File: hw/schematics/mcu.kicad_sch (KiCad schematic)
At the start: 10 parts, among them J3 TC2050-IDC, U1 ISP2454-LP-JT

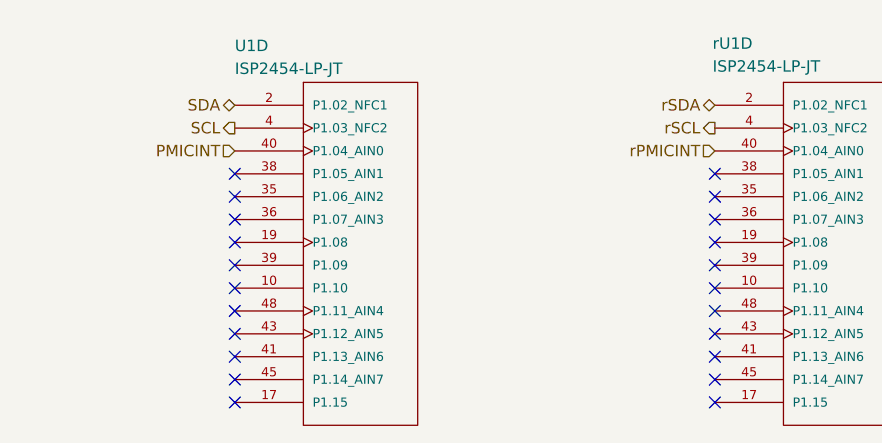
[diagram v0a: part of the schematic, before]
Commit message: Hook up matrix
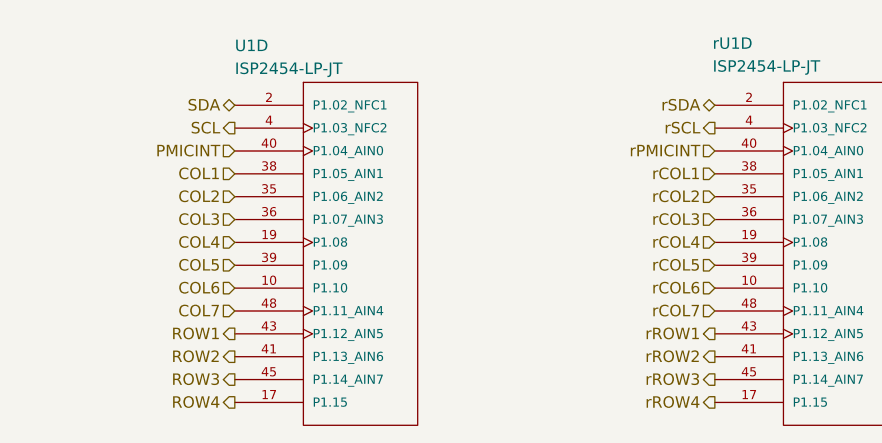
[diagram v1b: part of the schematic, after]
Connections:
- net COL6: now reaches U1.10 (P1.10)
- net ROW4: now reaches U1.17 (P1.15)
- net COL4: now reaches U1.19 (P1.08)
- net COL2: now reaches U1.35 (P1.06_AIN2)
- net COL3: now reaches U1.36 (P1.07_AIN3)
- net COL1: now reaches U1.38 (P1.05_AIN1)
- net COL5: now reaches U1.39 (P1.09)
- net ROW2: now reaches U1.41 (P1.13_AIN6)
- net ROW1: now reaches U1.43 (P1.12_AIN5)
- net ROW3: now reaches U1.45 (P1.14_AIN7)
- net COL7: now reaches U1.48 (P1.11_AIN4)
- net rCOL6: now reaches rU1.10 (P1.10)
- net rROW4: now reaches rU1.17 (P1.15)
- net rCOL4: now reaches rU1.19 (P1.08)
- net rCOL2: now reaches rU1.35 (P1.06_AIN2)
- net rCOL3: now reaches rU1.36 (P1.07_AIN3)
- net rCOL1: now reaches rU1.38 (P1.05_AIN1)
- net rCOL5: now reaches rU1.39 (P1.09)
- net rROW2: now reaches rU1.41 (P1.13_AIN6)
- net rROW1: now reaches rU1.43 (P1.12_AIN5)
- net rROW3: now reaches rU1.45 (P1.14_AIN7)
- net rCOL7: now reaches rU1.48 (P1.11_AIN4)
- no-connect marks 68 -> 46

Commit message: Annotate; Remove unused LDO/LS; Add RGB LED to PMIC
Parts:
- renumbered R15 to R12, R16 to R13, R17 to R14, rR15 to rR12, rR16 to rR13, rR17 to rR14
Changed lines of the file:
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@@
 		(on_board yes)
 		(dnp no)
-		(property "Reference" "rR15"
+		(property "Reference" "rR12"
 			(at 135.382 153.416 0)
 			(effects
@@
 			(project "alidade"
 				(path "/4cc5d416-57f5-4147-8183-e03ae6b1198a/43e81299-cad2-4202-975b-6352d1fdfcdc"
-					(reference "rR15")
+					(reference "rR12")
 					(unit 1)
 				)
@@
 		(on_board yes)
 		(dnp no)
-		(property "Reference" "rR17"
+		(property "Reference" "rR14"
 			(at 148.082 153.416 0)
 			(effects
@@
 			(project "alidade"
 				(path "/4cc5d416-57f5-4147-8183-e03ae6b1198a/43e81299-cad2-4202-975b-6352d1fdfcdc"
-					(reference "rR17")
+					(reference "rR14")
 					(unit 1)
 				)
@@
 		(on_board yes)
 		(dnp no)
-		(property "Reference" "rR16"
+		(property "Reference" "rR13"
 			(at 141.732 153.416 0)
 			(effects
@@
 			(project "alidade"
 				(path "/4cc5d416-57f5-4147-8183-e03ae6b1198a/43e81299-cad2-4202-975b-6352d1fdfcdc"
-					(reference "rR16")
+					(reference "rR13")
 					(unit 1)
 				)
@@
 		(on_board yes)
 		(dnp no)
-		(property "Reference" "R16"
+		(property "Reference" "R13"
 			(at 62.992 154.686 0)
 			(effects
@@
 			(project "alidade"
 				(path "/4cc5d416-57f5-4147-8183-e03ae6b1198a/43e81299-cad2-4202-975b-6352d1fdfcdc"
-					(reference "R16")
+					(reference "R13")
 					(unit 1)
 				)
@@
 		(on_board yes)
 		(dnp no)
-		(property "Reference" "R17"
+		(property "Reference" "R14"
 			(at 69.342 154.686 0)
 			(effects
@@
 			(project "alidade"
 				(path "/4cc5d416-57f5-4147-8183-e03ae6b1198a/43e81299-cad2-4202-975b-6352d1fdfcdc"
-					(reference "R17")
+					(reference "R14")
 					(unit 1)
 				)
@@
 		(on_board yes)
 		(dnp no)
-		(property "Reference" "R15"
+		(property "Reference" "R12"
 			(at 56.642 154.686 0)
 			(effects
@@
 			(project "alidade"
 				(path "/4cc5d416-57f5-4147-8183-e03ae6b1198a/43e81299-cad2-4202-975b-6352d1fdfcdc"
-					(reference "R15")
+					(reference "R12")
 					(unit 1)
 				)

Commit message: Rename power rails
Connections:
- net 1V8 renamed DVDD
- net r1V8 renamed rDVDD
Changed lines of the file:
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@@
 	)
 	(symbol
-		(lib_id "Alidade:r1V8")
+		(lib_id "Alidade:rDVDD")
 		(at 167.64 142.24 0)
 		(unit 1)
@@
 		(dnp no)
 		(fields_autoplaced yes)
-		(property "Reference" "#r1V8_08"
+		(property "Reference" "#rDVDD0110"
 			(at 167.64 146.05 0)
 			(effects
@@
 			)
 		)
-		(property "Value" "r1V8"
+		(property "Value" "rDVDD"
 			(at 167.64 137.16 0)
 			(effects
@@
 			(project "alidade"
 				(path "/4cc5d416-57f5-4147-8183-e03ae6b1198a/43e81299-cad2-4202-975b-6352d1fdfcdc"
-					(reference "#r1V8_08")
+					(reference "#rDVDD0110")
 					(unit 1)
 				)
@@
 	)
 	(symbol
-		(lib_id "Alidade:r1V8")
+		(lib_id "Alidade:rDVDD")
 		(at 80.01 44.45 0)
 		(unit 1)
@@
 		(dnp no)
 		(fields_autoplaced yes)
-		(property "Reference" "#r1V8_06"
+		(property "Reference" "#rDVDD0108"
 			(at 80.01 48.26 0)
 			(effects
@@
 			)
 		)
-		(property "Value" "r1V8"
+		(property "Value" "rDVDD"
 			(at 80.01 39.37 0)
 			(effects
@@
 			(project "alidade"
 				(path "/4cc5d416-57f5-4147-8183-e03ae6b1198a/43e81299-cad2-4202-975b-6352d1fdfcdc"
-					(reference "#r1V8_06")
+					(reference "#rDVDD0108")
 					(unit 1)
 				)
@@
 	)
 	(symbol
-		(lib_id "Alidade:r1V8")
+		(lib_id "Alidade:rDVDD")
 		(at 134.62 144.78 0)
 		(unit 1)
@@
 		(dnp no)
 		(fields_autoplaced yes)
-		(property "Reference" "#r1V8_07"
+		(property "Reference" "#rDVDD0109"
 			(at 134.62 148.59 0)
 			(effects
@@
 			)
 		)
-		(property "Value" "r1V8"
+		(property "Value" "rDVDD"
 			(at 134.62 139.7 0)
 			(effects
@@
 			(project "alidade"
 				(path "/4cc5d416-57f5-4147-8183-e03ae6b1198a/43e81299-cad2-4202-975b-6352d1fdfcdc"
-					(reference "#r1V8_07")
+					(reference "#rDVDD0109")
 					(unit 1)
 				)
@@
 	)
 	(symbol
-		(lib_id "Alidade:1V8")
+		(lib_id "Alidade:DVDD")
 		(at 55.88 146.05 0)
 		(unit 1)
@@
 		(dnp no)
 		(fields_autoplaced yes)
-		(property "Reference" "#1V8_08"
+		(property "Reference" "#DVDD0109"
 			(at 55.88 149.86 0)
 			(effects
@@
 			)
 		)
-		(property "Value" "1V8"
+		(property "Value" "DVDD"
 			(at 55.88 140.97 0)
 			(effects
@@
 			(project "alidade"
 				(path "/4cc5d416-57f5-4147-8183-e03ae6b1198a/43e81299-cad2-4202-975b-6352d1fdfcdc"
-					(reference "#1V8_08")
+					(reference "#DVDD0109")
 					(unit 1)
 				)
@@
 	)
 	(symbol
-		(lib_id "Alidade:1V8")
+		(lib_id "Alidade:DVDD")
 		(at 44.45 43.18 0)
 		(unit 1)
@@
 		(dnp no)
 		(fields_autoplaced yes)
-		(property "Reference" "#1V8_05"
+		(property "Reference" "#DVDD0108"
 			(at 44.45 46.99 0)
 			(effects
@@
 			)
 		)
-		(property "Value" "1V8"
+		(property "Value" "DVDD"
 			(at 44.45 38.1 0)
 			(effects
@@
 			(project "alidade"
 				(path "/4cc5d416-57f5-4147-8183-e03ae6b1198a/43e81299-cad2-4202-975b-6352d1fdfcdc"
-					(reference "#1V8_05")
+					(reference "#DVDD0108")
 					(unit 1)
 				)
@@
 	)
 	(symbol
-		(lib_id "Alidade:1V8")
+		(lib_id "Alidade:DVDD")
 		(at 88.9 143.51 0)
 		(unit 1)
@@
 		(dnp no)
 		(fields_autoplaced yes)
-		(property "Reference" "#1V8_07"
+		(property "Reference" "#DVDD0110"
 			(at 88.9 147.32 0)
 			(effects
@@
 			)
 		)
-		(property "Value" "1V8"
+		(property "Value" "DVDD"
 			(at 88.9 138.43 0)
 			(effects
@@
 			(project "alidade"
 				(path "/4cc5d416-57f5-4147-8183-e03ae6b1198a/43e81299-cad2-4202-975b-6352d1fdfcdc"
-					(reference "#1V8_07")
+					(reference "#DVDD0110")
 					(unit 1)
 				)

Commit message: Extra 0 ohm inline resistors
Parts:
- added R401, R402, R403, R404, R405, rR401, rR402, rR403, rR404, rR405: 0, symbol Alidade:R
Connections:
- net MOSI: now also R404.1; no longer U1.9 (P2.08_TRACEDATA1/SDO)
- net SCK: now also R405.1; no longer U1.15 (P2.06_TRACECLK/SCK)
- net SWCLK: now also R402.1; no longer J3.4 (SWDCLK)
- net SWDIO: now also R401.1; no longer J3.2 (SWDIO)
- net SWO: now also R403.1; no longer J3.6 (SWO)
- net rMOSI: now also rR404.1; no longer rU1.9 (P2.08_TRACEDATA1/SDO)
- net rSCK: now also rR405.1; no longer rU1.15 (P2.06_TRACECLK/SCK)
- net rSWCLK: now also rR402.1; no longer rJ3.4 (SWDCLK)
- net rSWDIO: now also rR401.1; no longer rJ3.2 (SWDIO)
- net rSWO: now also rR403.1; no longer rJ3.6 (SWO)
- new net: rR405.2, rU1.15 (P2.06_TRACECLK/SCK)
- new net: J3.6 (SWO), R403.2
- new net: rJ3.2 (SWDIO), rR401.2
- new net: rJ3.4 (SWDCLK), rR402.2
- new net: rJ3.6 (SWO), rR403.2
- new net: R404.2, U1.9 (P2.08_TRACEDATA1/SDO)
- new net: J3.2 (SWDIO), R401.2
- new net: R405.2, U1.15 (P2.06_TRACECLK/SCK)
- new net: rR404.2, rU1.9 (P2.08_TRACEDATA1/SDO)
- new net: J3.4 (SWDCLK), R402.2

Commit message: Use new switch for shphld
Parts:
- R401, R402, R403, R404, R405, rR401, rR402, rR403, rR404, rR405: footprint (none) -> Alidade:0603
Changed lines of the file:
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@@
 	(wire
 		(pts
-			(xy 87.4246 160.02) (xy 90.17 160.02)
+			(xy 87.63 160.02) (xy 90.17 160.02)
 		)
 		(stroke
@@
 	(wire
 		(pts
-			(xy 74.93 160.02) (xy 82.3446 160.02)
+			(xy 74.93 160.02) (xy 82.55 160.02)
 		)
 		(stroke
@@
 			)
 		)
-		(property "Footprint" ""
+		(property "Footprint" "Alidade:0603"
 			(at 227.33 81.28 0)
 			(effects
@@
 	(symbol
 		(lib_id "Alidade:R")
-		(at 84.8846 160.02 90)
+		(at 85.09 160.02 90)
 		(unit 1)
 		(exclude_from_sim no)
@@
 		(dnp no)
 		(property "Reference" "R403"
-			(at 84.8846 158.242 90)
+			(at 85.09 158.242 90)
 			(effects
 				(font
@@
 		)
 		(property "Value" "0"
-			(at 84.8846 161.798 90)
+			(at 85.09 161.798 90)
 			(do_not_autoplace yes)
 			(effects
@@
 			)
 		)
-		(property "Footprint" ""
-			(at 84.8846 160.02 0)
+		(property "Footprint" "Alidade:0603"
+			(at 85.09 160.02 0)
 			(effects
 				(font
@@
 		)
 		(property "Datasheet" ""
-			(at 84.8846 160.02 0)
+			(at 85.09 160.02 0)
 			(effects
 				(font
@@
 		)
 		(property "Description" ""
-			(at 84.8846 160.02 0)
+			(at 85.09 160.02 0)
 			(effects
 				(font
@@
 			)
 		)
-		(property "Footprint" ""
+		(property "Footprint" "Alidade:0603"
 			(at 163.83 153.67 0)
 			(effects
@@
 			)
 		)
-		(property "Footprint" ""
+		(property "Footprint" "Alidade:0603"
 			(at 149.86 77.47 0)
 			(effects
@@
 			)
 		)
-		(property "Footprint" ""
+		(property "Footprint" "Alidade:0603"
 			(at 163.83 158.75 0)
 			(effects
@@
 			)
 		)
-		(property "Footprint" ""
+		(property "Footprint" "Alidade:0603"
 			(at 163.83 148.59 0)
 			(effects
@@
 			)
 		)
-		(property "Footprint" ""
+		(property "Footprint" "Alidade:0603"
 			(at 85.09 149.86 0)
 			(effects
@@
 			)
 		)
-		(property "Footprint" ""
+		(property "Footprint" "Alidade:0603"
 			(at 227.33 76.2 0)
 			(effects
@@
 			)
 		)
-		(property "Footprint" ""
+		(property "Footprint" "Alidade:0603"
 			(at 149.86 82.55 0)
 			(effects
@@
 			)
 		)
-		(property "Footprint" ""
+		(property "Footprint" "Alidade:0603"
 			(at 85.09 154.94 0)
 			(effects

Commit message: Switch mcu
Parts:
- removed U1: ISP2454-LP-JT, Alidade:XCVR_ISP2454-LX-JT, symbol Alidade:ISP2454-LP-JT
- removed unit 1 of rU1
- removed unit 5 of rU1
- added C401, C402, C403, C404: 100n, symbol Alidade:C
- added C405: 10u, symbol Alidade:C
- added C406, C407: 2.2u, symbol Alidade:C
- added C408: 10n, symbol Alidade:C
- added C409: 2.2n, symbol Alidade:C
- added FB401: FB, symbol Alidade:FB
- added L401: L, symbol Alidade:L
- added U401: NRF54L15-QFAA-R, Alidade:QFN48_6X6_NOR, symbol Alidade:NRF54L15-QFAA-R
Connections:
- net ADCCS: now also U401.16 (P2.05/SPI.CS)
- net COL1: now also U401.5 (P1.04/AIN0/TAMPC)
- net COL2: now also U401.6 (P1.05/AIN1/TAMPC)
- net COL3: now also U401.7 (P1.06/AIN2/TAMPC)
- net COL4: now also U401.8 (P1.07/AIN3/TAMPC)
- net COL5: now also U401.9 (P1.08/CLK16M/TAMPC)
- net COL6: now also U401.37 (P1.09/TAMPC)
- net COL7: now also U401.38 (P1.10/TAMPC)
- net DRDY: now also U401.14 (P2.03)
- net DVDD: now also C401.1, C402.1, C403.1, C404.1, C405.1, U401.10 (VDD), U401.22 (VDD), U401.36 (VDD), U401.47 (VDD), U401.48 (VDD)
- net FAULT: now also U401.11 (P2.00/SPI.DCX)
- net GND: now also C401.2, C402.2, C403.2, C404.2, C405.2, C406.2, C407.2, C408.2, C409.2, U401.44 (VSS), U401.49 (VSS)
- net MISO: now also U401.13 (P2.02/SPI.SDI/SDO)
- net NRST: now also U401.30 (NRESET)
- net PMICINT: now also U401.27 (P0.02)
- net ROW1: now also U401.39 (P1.11/AIN4)
- net ROW2: now also U401.40 (P1.12/AIN5)
- net ROW3: now also U401.41 (P1.13/AIN6)
- net ROW4: now also U401.42 (P1.14/AIN7)
- net SCL: now also U401.29 (P0.04/GRTC_CLKOUT32K)
- net SDA: now also U401.28 (P0.03/GRTC_PWMOUT)
- net SWCLK: now also U401.26 (SWDCLK)
- net SWDIO: now also U401.25 (SWDIO)
- net SWO: now also U401.18 (P2.07/TRACEDATA[0]/SWO/SPI.DCX)
- net at R404.2: now also U401.15 (P2.04/SPI.SDI/SDO)
- net at R405.2: now also U401.12 (P2.01/SPI.SCK)
- new net: C406.1, FB401.1, L401.1, U401.45 (DECD)
- new net: L401.2, U401.46 (DCC)
- new net: C407.1, C408.1, C409.1, FB401.2, U401.33 (DECRF), U401.43 (DECA)
- no-connect marks 46 -> 3
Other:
- note added: "Antenna and Oscillator"
- note added: "Port 1"
- note added: "Port 2 and Debug"
- note added: "Power and decoupling"
- note removed: "Debug and FPGA SPI Labels are from FPGA perspective"
- note removed: "NC/Mechanical pads"
- note removed: "Port 1 PMICSDA/SCL pulled up on PMIC sheet"
- note removed: "Power No decoupling, integrated in SIP OUT_MOD connected to OUT_ANT"
- moved on the sheet: J3, R12, R13, R14, R401, R402, R403, R404, R405, rJ3, rR12, rR13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

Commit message: Second mcu and reset refs
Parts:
- removed rR404, rR405: 0, Alidade:0603, symbol Alidade:R
- removed rU1: ISP2454-LP-JT, Alidade:XCVR_ISP2454-LX-JT, symbol Alidade:ISP2454-LP-JT
- added ANT?, rANT?: ~, symbol Alidade:SWRA117D
- added C?, rC?: 2p, symbol Alidade:C
- added C?, rC?: 0.3p, symbol Alidade:C
- added C?, rC?: 1.5p, symbol Alidade:C
- added L? (x2), rL? (x2): 3.5n, symbol Alidade:L
- added L?, rL?: 2.7n, symbol Alidade:L
- added TP? (x5), rTP? (x5): TestPoint, symbol Alidade:TestPoint
- added Y?, rY?: 32M, symbol Alidade:Crystal_GND24
- added Y?, rY?: 32.768K, symbol Alidade:Crystal_GND24
- added rC? (x4): 100n, symbol Alidade:C
- added rC?: 10n, symbol Alidade:C
- added rC?: 2.2n, symbol Alidade:C
- added rC? (x2): 2.2u, symbol Alidade:C
- added rC?: 10u, symbol Alidade:C
- added rFB?: FB, symbol Alidade:FB
- added rL?: 4.7u, symbol Alidade:L
- added rR? (x2): 0, Alidade:0603, symbol Alidade:R
- added rU? (x6): NRF54L15-QFAA-R, Alidade:QFN48_6X6_NOR, symbol Alidade:NRF54L15-QFAA-R
- L?: renamed from L401; value L -> 4.7u
- renumbered C409 to C?, C403 to C?, C404 to C?, C402 to C?, C407 to C?, C406 to C?, C408 to C?, C401 to C?, C405 to C?, FB401 to FB?, J3 to J?, R403 to R?, R404 to R?, R401 to R?, R405 to R?, R13 to R?, R402 to R?, R14 to R?, R12 to R?, U401 to U?, rJ3 to rJ?, rR12 to rR?, rR402 to rR?, rR403 to rR?, rR401 to rR?, rR14 to rR?, rR13 to rR?
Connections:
- net GND: now also U?.32 (VSS_PA), ANT?.2 (GND), C?.2, C?.2, C?.2, Y?.2, Y?.2, Y?.4, Y?.4, rANT?.2 (GND), rC?.2, rC?.2, rC?.2, rU?.32 (VSS_PA), rY?.2, rY?.4
- net SWO: now also TP?.1
- net rADCCS: now also rU?.16 (P2.05/SPI.CS)
- net rCOL1: now also rU?.5 (P1.04/AIN0/TAMPC)
- net rCOL2: now also rU?.6 (P1.05/AIN1/TAMPC)
- net rCOL3: now also rU?.7 (P1.06/AIN2/TAMPC)
- net rCOL4: now also rU?.8 (P1.07/AIN3/TAMPC)
- net rCOL5: now also rU?.9 (P1.08/CLK16M/TAMPC)
- net rCOL6: now also rU?.37 (P1.09/TAMPC)
- net rCOL7: now also rU?.38 (P1.10/TAMPC)
- net rDRDY: now also rU?.14 (P2.03)
- net rDVDD: now also rC?.1, rC?.1, rC?.1, rC?.1, rC?.1, rU?.10 (VDD), rU?.22 (VDD), rU?.36 (VDD), rU?.47 (VDD), rU?.48 (VDD)
- net rFAULT: now also rU?.11 (P2.00/SPI.DCX)
- net rGND: now also rC?.2, rC?.2, rC?.2, rC?.2, rC?.2, rC?.2, rC?.2, rC?.2, rC?.2, rU?.44 (VSS), rU?.49 (VSS), rY?.2, rY?.4
- net rMISO: now also rU?.13 (P2.02/SPI.SDI/SDO)
- net rMOSI: now also rR?.1
- net rNRST: now also rU?.30 (NRESET)
- net rPMICINT: now also rU?.27 (P0.02)
- net rROW1: now also rU?.39 (P1.11/AIN4)
- net rROW2: now also rU?.40 (P1.12/AIN5)
- net rROW3: now also rU?.41 (P1.13/AIN6)
- net rROW4: now also rU?.42 (P1.14/AIN7)
- net rSCK: now also rR?.1
- net rSCL: now also rU?.29 (P0.04/GRTC_CLKOUT32K)
- net rSDA: now also rU?.28 (P0.03/GRTC_PWMOUT)
- net rSWCLK: now also rU?.26 (SWDCLK)
- net rSWDIO: now also rU?.25 (SWDIO)
- net rSWO: now also rTP?.1, rU?.18 (P2.07/TRACEDATA[0]/SWO/SPI.DCX)
- net at U?.31 (ANT): now also L?.2
- net at U?.34 (XC1): now also Y?.3
- net at U?.35 (XC2): now also Y?.1
- net at U?.1 (P1.00/XL1): now also Y?.3
- net at U?.2 (P1.01/XL2): now also Y?.1
- net at U?.17 (P2.06/TRACECLK/SPI.SCK): now also TP?.1
- net at U?.19 (P2.08/TRACEDATA[1]/SPI.SDI/SDO): now also TP?.1
- net at U?.20 (P2.09/TRACEDATA[2]/SPI.SDI/SDO): now also TP?.1
- net at U?.21 (P2.10/TRACEDATA[3]/SPIM.CS): now also TP?.1
- new net: rR?.2, rU?.15 (P2.04/SPI.SDI/SDO)
- new net: rU?.1 (P1.00/XL1), rY?.3
- new net: rU?.2 (P1.01/XL2), rY?.1
- new net: rR?.2, rU?.12 (P2.01/SPI.SCK)
- new net: rTP?.1, rU?.17 (P2.06/TRACECLK/SPI.SCK)
- new net: rTP?.1, rU?.19 (P2.08/TRACEDATA[1]/SPI.SDI/SDO)
- new net: rTP?.1, rU?.20 (P2.09/TRACEDATA[2]/SPI.SDI/SDO)
- new net: rTP?.1, rU?.21 (P2.10/TRACEDATA[3]/SPIM.CS)
- new net: C?.1, L?.1, L?.2 (x2)
- new net: rC?.1, rFB?.1, rL?.1, rU?.45 (DECD)
- new net: rC?.1, rC?.1, rC?.1, rFB?.2, rU?.33 (DECRF), rU?.43 (DECA)
- new net: rU?.35 (XC2), rY?.1
- new net: rU?.34 (XC1), rY?.3
- new net: ANT?.1 (FEED), C?.1, L?.1
- new net: rANT?.1 (FEED), rC?.1, rL?.1
- new net: rC?.1, rL?.1, rL?.2 (x2)
- new net: rL?.2, rU?.31 (ANT)
- new net: rL?.2, rU?.46 (DCC)
- no-connect marks 3 -> 8
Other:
- note added: "To 32"
- moved on the sheet: R?, U?E

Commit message: Refs and cleanup
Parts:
- gave numbers to parts that had none: 70
